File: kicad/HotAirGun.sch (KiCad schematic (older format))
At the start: 60 parts, among them CN1 220Vin, CN3 Trasf, CN5 Ventola, CN6 Conn Vite 1,5x2, J2 Reset, U3 TLP672-2, U4 Opto TRIAC Dip6

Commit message: Aggiornamento componenti e inclusione nell'archivio del cache libreria
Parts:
- F1: symbol FUSE -> Fuse
- L1: symbol INDUCTOR -> L_Core_Iron
- PR2: symbol Diode_Bridge -> D_Bridge_+AA-
- Pot1: symbol Coded_Switch -> Rotary_Encoder_Switch
- TR1: symbol TRIAC -> Q_TRIAC_AAG
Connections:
- wire segments 144 -> 167
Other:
- moved on the sheet: PT1
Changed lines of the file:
@@
 LIBS:contrib
 LIBS:valves
-LIBS:HotAriGun
-LIBS:HotAriGun-SchDoc-cache
-EELAYER 25 0
+LIBS:HotAirGun-cache
+EELAYER 26 0
 EELAYER END
 $Descr B 17000 11000
@@
 $EndComp
 $Comp
-L 12V #12V021
+L +12V #12V021
 U 1 1 58DBE2DA
 P 7000 5100
 F 0 "#12V021" H 7000 4950 50  0001 C CNN
-F 1 "12V" H 7000 5250 50  0000 C CNN
+F 1 "+12V" H 7000 5250 50  0000 C CNN
 F 2 "" H 7000 5100 60  0000 C CNN
 F 3 "" H 7000 5100 60  0000 C CNN
@@
 $EndComp
 $Comp
-L 12V #12V_025
+L +12V #12V_025
 U 1 1 58DBE2D6
 P 9200 5300
 F 0 "#12V_025" H 9200 5150 50  0001 C CNN
-F 1 "12V" H 9200 5450 50  0000 C CNN
+F 1 "+12V" H 9200 5450 50  0000 C CNN
 F 2 "" H 9200 5300 60  0000 C CNN
 F 3 "" H 9200 5300 60  0000 C CNN
@@
 V1.1
 $Comp
-L Coded_Switch Pot1
+L Rotary_Encoder_Switch Pot1
 U 1 1 58DBE2C6
 P 7200 2550
@@
 F 3 "" H 7800 3800 50  0000 C CNN
 	1    7800 3800
-	0    1    1    0
+	1    0    0    -1
 $EndComp
 $Comp
@@
 $EndComp
 $Comp
-L Diode_Bridge PR2
+L D_Bridge_+AA- PR2
 U 1 1 58DBE2AD
 P 2650 7000
 F 0 "PR2" V 3000 7250 50  0000 C CNN
-F 1 "PontRaddr 2A" V 2350 6700 50  0000 C CNN
+F 1 "PontRaddr 2A" V 2420 6730 50  0000 C CNN
 F 2 "" H 2650 7000 50  0000 C CNN
 F 3 "" H 2650 7000 50  0000 C CNN
@@
 $EndComp
 $Comp
-L INDUCTOR L1
+L L_Core_Iron L1
 U 1 1 58DBE2AB
-P 3150 8100
-F 0 "L1" V 3100 8100 50  0000 C CNN
-F 1 "~" V 3250 8100 50  0000 C CNN
-F 2 "" H 3150 8100 50  0000 C CNN
-F 3 "" H 3150 8100 50  0000 C CNN
-	1    3150 8100
-	-1   0    0    1
-$EndComp
-$Comp
-L TRIAC TR1
+P 3150 8540
+F 0 "L1" V 3100 8540 50  0000 C CNN
+F 1 "~" V 3250 8540 50  0000 C CNN
+F 2 "" H 3150 8540 50  0000 C CNN
+F 3 "" H 3150 8540 50  0000 C CNN
+	1    3150 8540
+	-1   0    0    1
+$EndComp
+$Comp
+L Q_TRIAC_AAG TR1
 U 1 1 58DBE2AA
-P 3150 8850
-F 0 "TR1" H 2900 9200 50  0000 C CNN
-F 1 "~" H 2850 8600 50  0000 C CNN
-F 2 "" H 3150 8850 50  0000 C CNN
-F 3 "" H 3150 8850 50  0000 C CNN
-	1    3150 8850
+P 3150 8950
+F 0 "TR1" H 125 25  50  0000 L CNN
+F 1 "~" H 125 -50 50  0000 L CNN
+F 2 "" V 75  25  50  0001 C CNN
+F 3 "" V 0   0   50  0001 C CNN
+	1    3150 8950
 	1    0    0    -1
 $EndComp
@@
 $EndComp
 $Comp
-L FUSE F1
+L Fuse F1
 U 1 1 58DBE29E
 P 4650 8700
-F 0 "F1" H 4750 8750 50  0000 C CNN
-F 1 "Fuse1" H 4550 8650 50  0000 C CNN
+F 0 "F1" V 4570 8640 50  0000 C CNN
+F 1 "Fuse1" V 4710 8700 50  0000 C CNN
 F 2 "" H 4650 8700 50  0000 C CNN
 F 3 "" H 4650 8700 50  0000 C CNN
 	1    4650 8700
-	1    0    0    -1
+	0    1    1    0
 $EndComp
 $Comp
@@
 RA4
 Wire Wire Line
-	4500 5600 5200 5600
+	4500 5600 5000 5600
+Wire Wire Line
+	5000 5600 5200 5600
 Wire Wire Line
 	5000 2900 5000 5600
@@
 	3000 2800 5100 2800
 Wire Wire Line
-	2400 3600 3300 3600
+	2400 3600 3100 3600
+Wire Wire Line
+	3100 3600 3300 3600
 Wire Wire Line
 	2400 3900 2400 3600
@@
 	4700 3600 4700 4100
 Wire Wire Line
-	3600 3600 4700 3600
+	3600 3600 4000 3600
+Wire Wire Line
+	4000 3600 4700 3600
 Wire Wire Line
 	3000 2700 3000 2800
@@
 	2200 4000 2500 4000
 Wire Wire Line
-	2200 3250 2200 4000
+	2200 3250 2200 3400
+Wire Wire Line
+	2200 3400 2200 4000
 Wire Wire Line
 	3100 2700 3100 2900
@@
 	7950 3800 8700 3800
 Wire Wire Line
-	9700 3400 9700 3900
+	9700 3400 9700 3800
+Wire Wire Line
+	9700 3800 9700 3900
 Wire Wire Line
 	8900 3400 8900 3800
@@
 	7000 6100 7400 6100
 Wire Wire Line
-	7000 5300 7000 5600
+	7000 5300 7000 5500
+Wire Wire Line
+	7000 5500 7000 5600
 Wire Wire Line
 	3700 7100 3250 7100
 Wire Wire Line
-	2700 7700 3350 7700
-Wire Wire Line
-	2700 8250 2700 7700
+	2700 8140 3150 8140
+Wire Wire Line
+	3150 8140 3350 8140
 Connection ~ 7000 5500
 Connection ~ 6200 5800
 Wire Wire Line
-	7000 6000 7000 6200
+	7000 6000 7000 6100
+Wire Wire Line
+	7000 6100 7000 6200
 Connection ~ 7000 6100
 Connection ~ 12100 3000
 Connection ~ 12500 3000
 Connection ~ 6100 3050
-Connection ~ 3150 7700
+Connection ~ 3150 8140
 Connection ~ 5000 5600
 Wire Wire Line
 	9500 7100 9800 7100
 Wire Wire Line
-	9500 7100 9500 7550
+	9500 7100 9500 7450
+Wire Wire Line
+	9500 7450 9500 7550
 Wire Wire Line
 	10500 7100 10100 7100
 Wire Wire Line
-	10400 7450 10650 7450
-Wire Wire Line
-	10500 7100 10500 7550
+	10400 7450 10500 7450
+Wire Wire Line
+	10500 7450 10650 7450
+Wire Wire Line
+	10500 7100 10500 7450
+Wire Wire Line
+	10500 7450 10500 7550
 Connection ~ 9500 7450
 Connection ~ 10500 7450
@@
 	1700 3000 1700 3050
 Wire Wire Line
-	1700 3350 1700 3450
+	1700 3350 1700 3400
+Wire Wire Line
+	1700 3400 1700 3450
 Wire Wire Line
 	1800 3400 1700 3400
@@
 	5600 4100 5600 3650
 Wire Wire Line
-	6000 3650 6000 3750
-Wire Wire Line
-	6300 3650 6300 3750
+	6000 3650 6000 3700
+Wire Wire Line
+	6000 3700 6000 3750
+Wire Wire Line
+	6300 3650 6300 3700
+Wire Wire Line
+	6300 3700 6300 3750
 Wire Wire Line
 	6350 3700 6300 3700
@@
 	6100 3000 6100 3050
 Wire Wire Line
-	5950 3050 6250 3050
-Wire Wire Line
-	2650 6600 3250 6600
-Wire Wire Line
-	3250 6600 3250 6900
+	5950 3050 6100 3050
+Wire Wire Line
+	6100 3050 6250 3050
+Wire Wire Line
+	2650 6700 3250 6700
+Wire Wire Line
+	3250 6700 3250 6900
 Wire Wire Line
 	3250 6900 3350 6900
@@
 	3650 6900 3700 6900
 Wire Wire Line
-	3250 7100 3250 7400
-Wire Wire Line
-	3250 7400 2650 7400
-Wire Wire Line
-	2150 7000 2250 7000
-Wire Wire Line
-	2150 6500 3050 6500
-Wire Wire Line
-	3050 6500 3050 7000
+	3250 7100 3250 7300
+Wire Wire Line
+	3250 7300 2650 7300
+Wire Wire Line
+	2150 7000 2350 7000
+Wire Wire Line
+	2150 6500 2950 6500
+Wire Wire Line
+	2950 6500 2950 7000
 Wire Wire Line
 	1700 3000 1600 3000
@@
 	4350 8800 5250 8800
 Wire Wire Line
-	4950 8700 4900 8700
-Wire Wire Line
-	4400 8700 4350 8700
+	4950 8700 4800 8700
+Wire Wire Line
+	4500 8700 4350 8700
 Wire Wire Line
 	4700 8250 4350 8250
@@
 	10500 7900 10500 7850
 Wire Wire Line
-	9350 7450 9600 7450
+	9350 7450 9500 7450
+Wire Wire Line
+	9500 7450 9600 7450
 Wire Wire Line
 	9500 7900 9500 7850
@@
 	11900 5600 11950 5600
 Wire Wire Line
-	12250 5600 12450 5600
+	12250 5600 12400 5600
+Wire Wire Line
+	12400 5600 12450 5600
 Wire Wire Line
 	12400 6100 12450 6100
@@
 	11950 6200 11900 6200
 Wire Wire Line
-	12250 6200 12450 6200
+	12250 6200 12400 6200
+Wire Wire Line
+	12400 6200 12450 6200
 Wire Wire Line
 	12400 6250 12400 6200
@@
 	7400 5500 7400 5600
 Wire Wire Line
-	6100 5800 6350 5800
+	6100 5800 6200 5800
+Wire Wire Line
+	6200 5800 6350 5800
 Wire Wire Line
 	6200 5850 6200 5800
@@
 	12100 3000 12150 3000
 Wire Wire Line
-	12450 3000 12650 3000
+	12450 3000 12500 3000
+Wire Wire Line
+	12500 3000 12650 3000
 Text GLabel 12100 2850 1    60   Input ~ 0
 TC+
 Wire Wire Line
-	12100 2850 12100 3200
+	12100 2850 12100 3000
+Wire Wire Line
+	12100 3000 12100 3200
 Text GLabel 12500 2850 1    60   Input ~ 0
 TC-
 Wire Wire Line
-	12500 2850 12500 3200
+	12500 2850 12500 3000
+Wire Wire Line
+	12500 3000 12500 3200
 Text GLabel 12100 4200 3    60   Input ~ 0
 RC2
@@
 	2700 8850 2700 8550
 Wire Wire Line
-	2300 9050 2650 9050
+	2300 9050 3000 9050
 Wire Wire Line
 	3300 9200 3150 9200
@@
 	3050 9300 3300 9300
 Wire Wire Line
-	3150 7700 3150 7800
-Text GLabel 3350 7700 2    60   Input ~ 0
+	3150 8140 3150 8390
+Text GLabel 3350 8140 2    60   Input ~ 0
 220F
 Wire Wire Line
@@
 Text Notes 12100 3600 0    60   ~ 0
 MAX6675
+Wire Wire Line
+	2700 8140 2700 8250
+Wire Wire Line
+	3150 8690 3150 8800
 $EndSCHEMATC

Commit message: Modifica dimensione pagina foglio schema elettrico settato A4 per migliorare la stampa, aggiornamento informazioni sul foglio
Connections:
- net labels removed: 12V
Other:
- note removed: "HotAriGun"
- note removed: "V1.1"
- moved on the sheet: A, B, C1, C10, C11, C2, C3, C4, CN, CN1, CN2, CN3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

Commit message: Modifica README.md, pubblicazione schemi
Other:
- note removed: "Msystem"
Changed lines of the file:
@@
 LIBS:valves
 LIBS:HotAirGun-cache
-EELAYER 26 0
+EELAYER 25 0
 EELAYER END
 $Descr A4 11693 8268
@@
 U 1 1 58DBE2AA
 P 3070 7240
-F 0 "TR1" H 45  -1685 50  0000 L CNN
+F 0 "TR1" H 3120 7290 50  0000 L CNN
 F 1 "~" H 45  -1760 50  0000 L CNN
 F 2 "" V -5  -1685 50  0001 C CNN
@@
 Wire Wire Line
 	3070 6980 3070 7090
-Text Notes 13000 9300 0    60   ~ 0
-Msystem
 $EndSCHEMATC

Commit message: Schema aggiornato con arduino nano
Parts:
- removed C1, C2: ~, symbol C
- removed Y1: ~, symbol Crystal
- added J?: Arduino_Nano_Header, symbol Arduino_Nano_Header
- added U?: MAX6675, symbol MAX6675
- LD1, LD2, LD3, LD4: symbol LED -> LED-RESCUE-HotAirGun
- PT1: symbol POT -> POT-RESCUE-HotAirGun
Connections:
- net labels added: A6, A7, CLK, CS, DO, FAN, FASE_0, RELE_SIC_220V, SCL, SDA, SO, TRIAC
- net labels removed: +GND, +VCC, RB0, RC0, RC1, RC2, RC3, RC5, RC6
- wire segments 167 -> 163
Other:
- note removed: "MAX6675"
- note removed: "PIC16F877"

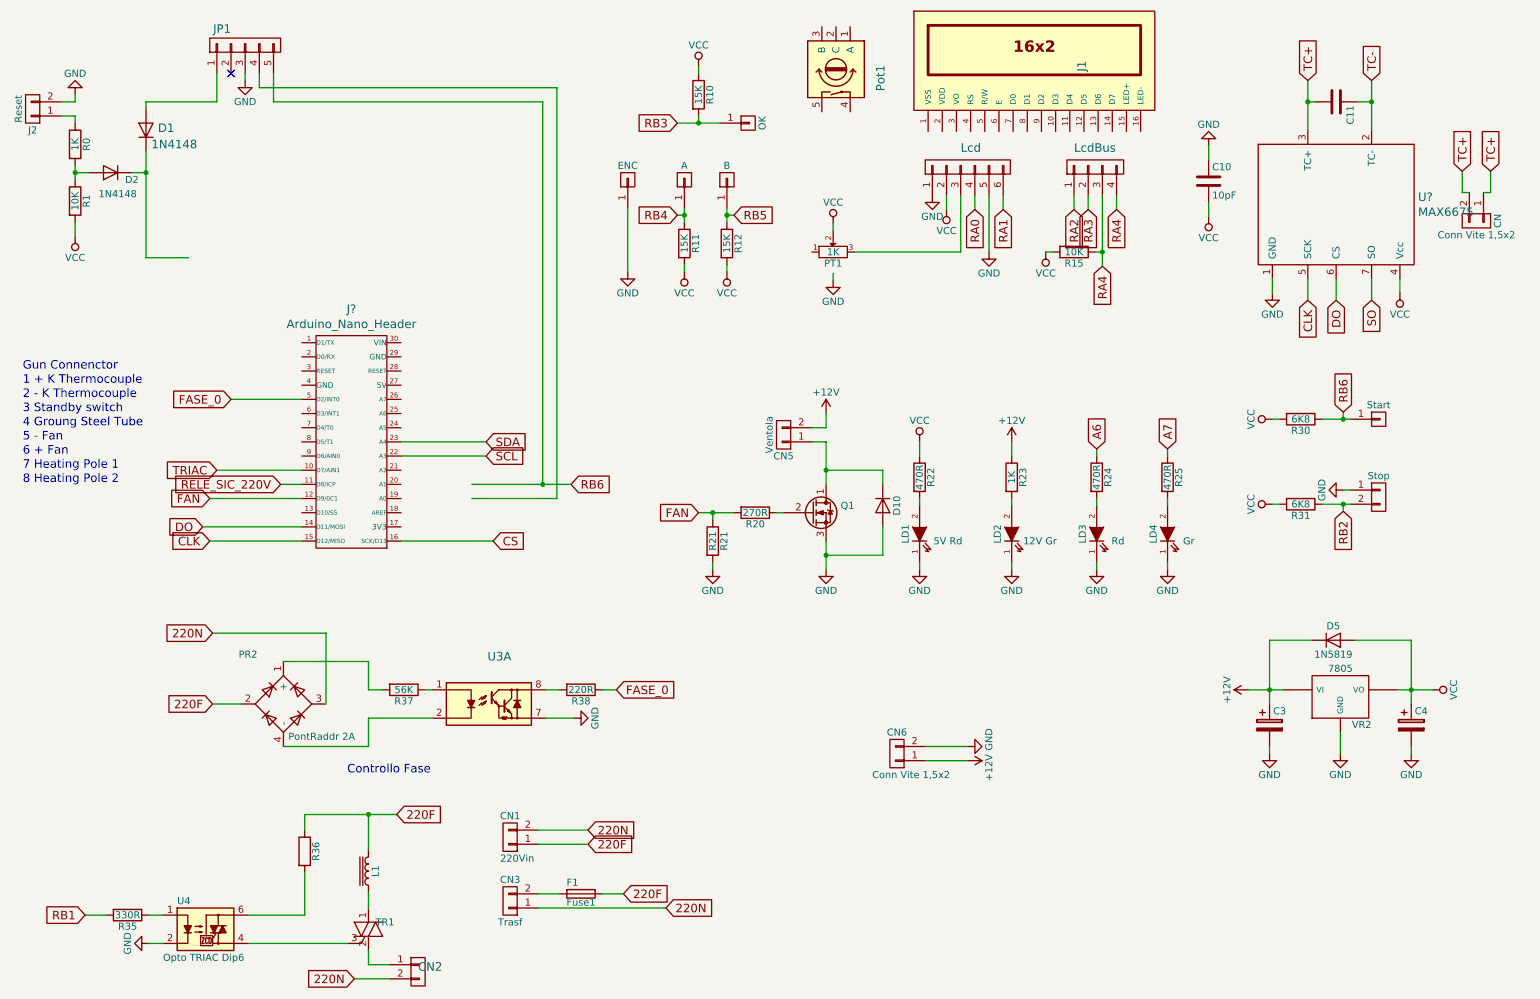
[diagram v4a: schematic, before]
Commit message: Schematic update pullup for int pin
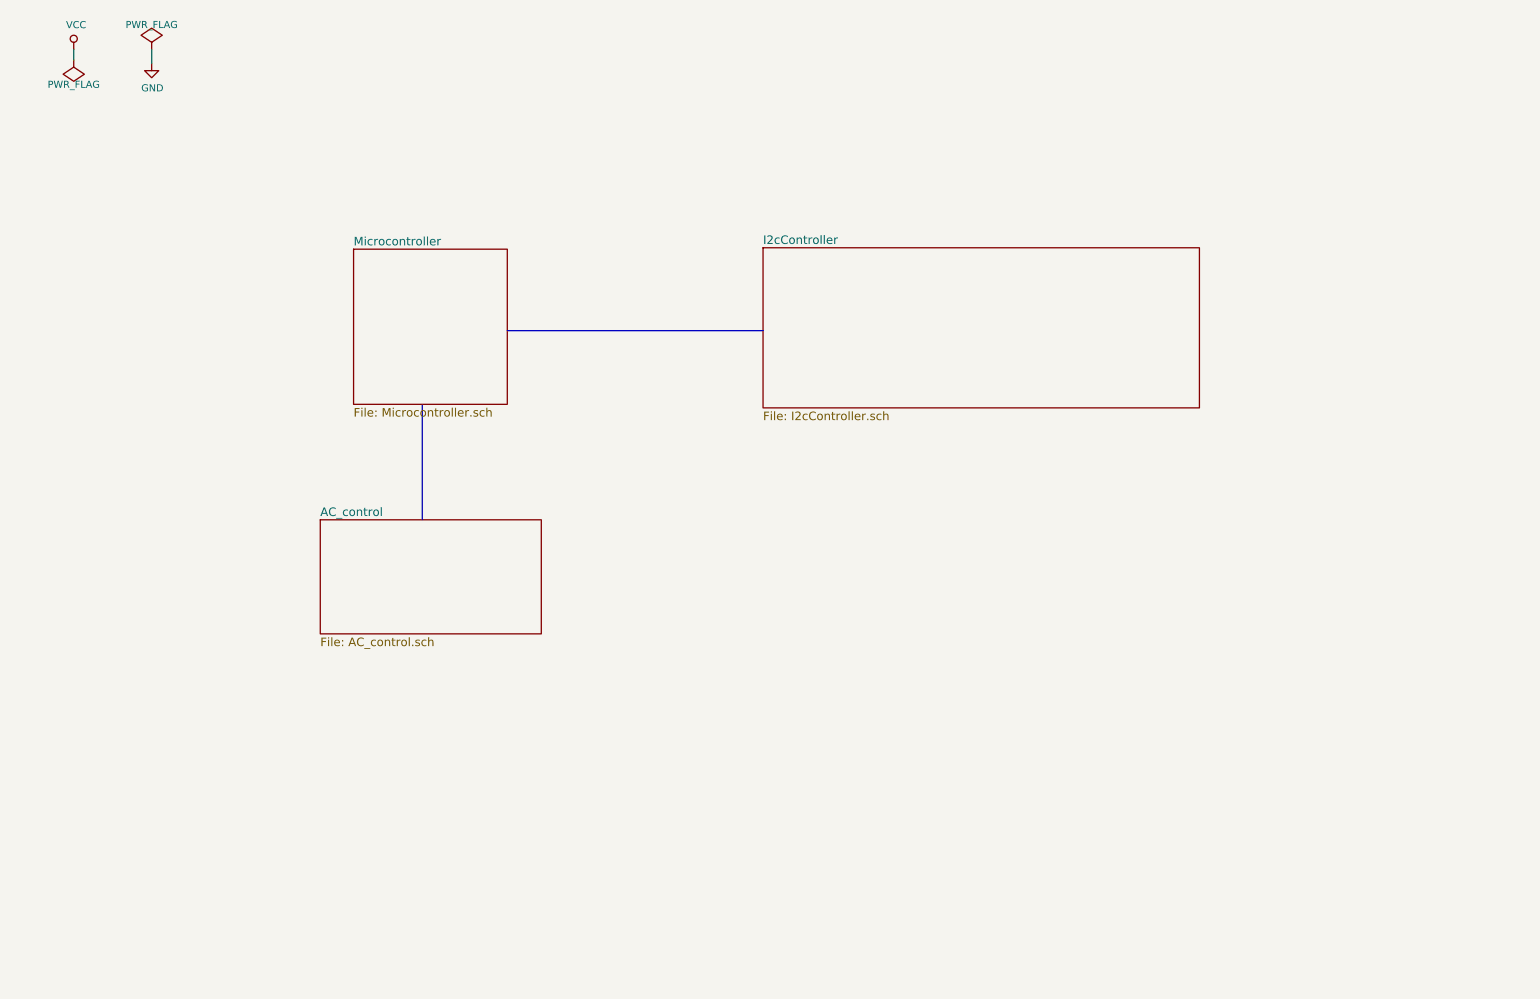
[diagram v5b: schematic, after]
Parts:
- removed A, B, ENC, OK: CONN_01X01, symbol CONN_01X01
- removed C10: 10pF, symbol C
- removed C11: ~, symbol C
- removed C3, C4: ~, symbol CP
- removed CN, CN6: Conn Vite 1,5x2, symbol CONN_01X02
- removed CN1: 220Vin, symbol CONN_01X02
- removed CN2, Stop: ~, symbol CONN_01X02
- removed CN3: Trasf, symbol CONN_01X02
- removed CN5: Ventola, symbol CONN_01X02
- removed D1, D2: 1N4148, symbol D
- removed D10: ~, symbol D
- removed D5: 1N5819, symbol D
- removed F1: Fuse1, symbol Fuse
- removed J1: ~, symbol LCD-016N002L
- removed J2: Reset, symbol CONN_01X02
- removed J?: Arduino_Nano_Header, symbol Arduino_Nano_Header
- removed JP1: ~, symbol CONN_01X05
- removed L1: ~, symbol L_Core_Iron
- removed LD1: 5V Rd, symbol LED-RESCUE-HotAirGun
- removed LD2: 12V Gr, symbol LED-RESCUE-HotAirGun
- removed LD3: Rd, symbol LED-RESCUE-HotAirGun
- removed LD4: Gr, symbol LED-RESCUE-HotAirGun
- removed Lcd: ~, symbol CONN_01X06
- removed LcdBus: ~, symbol CONN_01X04
- removed PR2: PontRaddr 2A, symbol D_Bridge_+AA-
- removed PT1: 1K, symbol POT-RESCUE-HotAirGun
- removed Pot1: ~, symbol Rotary_Encoder_Switch
- removed Q1: ~, symbol Q_NMOS_DGS
- removed R0, R23: 1K, symbol R
- removed R1, R15: 10K, symbol R
- removed R10, R11, R12: 15K, symbol R
- removed R20: 270R, symbol R
- removed R21: R21, symbol R
- removed R22, R24, R25: 470R, symbol R
- removed R30, R31: 6K8, symbol R
- removed R35: 330R, symbol R
- removed R36: ~, symbol R
- removed R37: 56K, symbol R
- removed R38: 220R, symbol R
- removed Start: ~, symbol CONN_01X01
- removed TR1: ~, symbol Q_TRIAC_AAG
- removed U3: TLP672-2, symbol TLP627-2
- removed U4: Opto TRIAC Dip6, symbol MOC3032M
- removed U?: MAX6675, symbol MAX6675
- removed VR2: 7805, symbol 7805
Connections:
- no-connect marks 1 -> 0
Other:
- note removed: "1 + K Thermocouple"
- note removed: "2 - K Thermocouple"
- note removed: "3 Standby switch"
- note removed: "4 Groung Steel Tube"
- note removed: "5 - Fan"
- note removed: "6 + Fan"
- note removed: "7 Heating Pole 1"
- note removed: "8 Heating Pole 2"
- note removed: "Controllo Fase"
- note removed: "Gun Connenctor"
